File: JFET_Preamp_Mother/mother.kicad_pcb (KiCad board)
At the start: 2 copper layers, 80 x 120 mm, 90 parts, among them J101 Conn_01x02, J102 Conn_01x08_Socket, J201 XLR3, J301 XLR3, J401 XLR3, J501 XLR3, Q201 2SK209, Q202 2SK209, Q203 2SK209, Q301 2SK209, Q302 2SK209, Q303 2SK209, Q401 2SK209, Q402 2SK209, Q403 2SK209, Q501 2SK209, Q502 2SK209, Q503 2SK209, U101 PCM1865DBTR, U102 TLV70012_SOT23-5

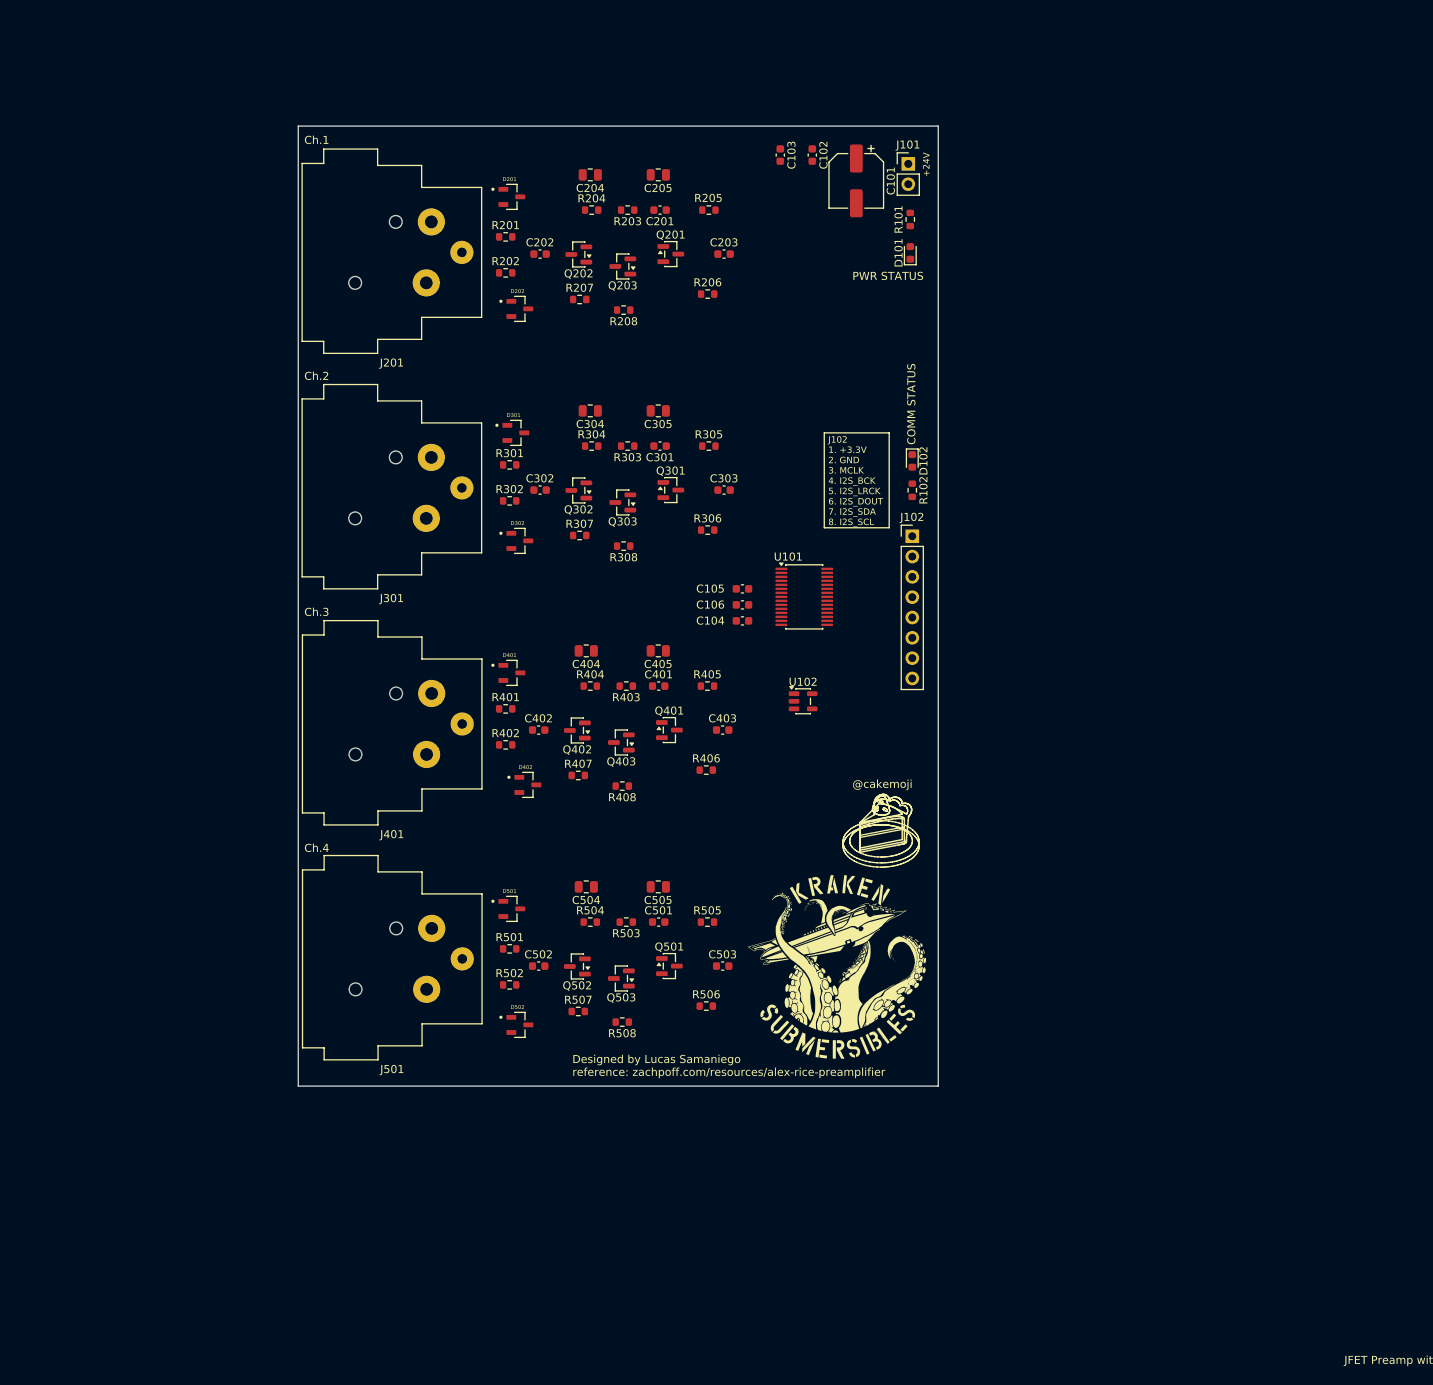
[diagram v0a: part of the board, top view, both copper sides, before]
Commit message: fix ERC on schematic, then proceed to begin routing on pcb
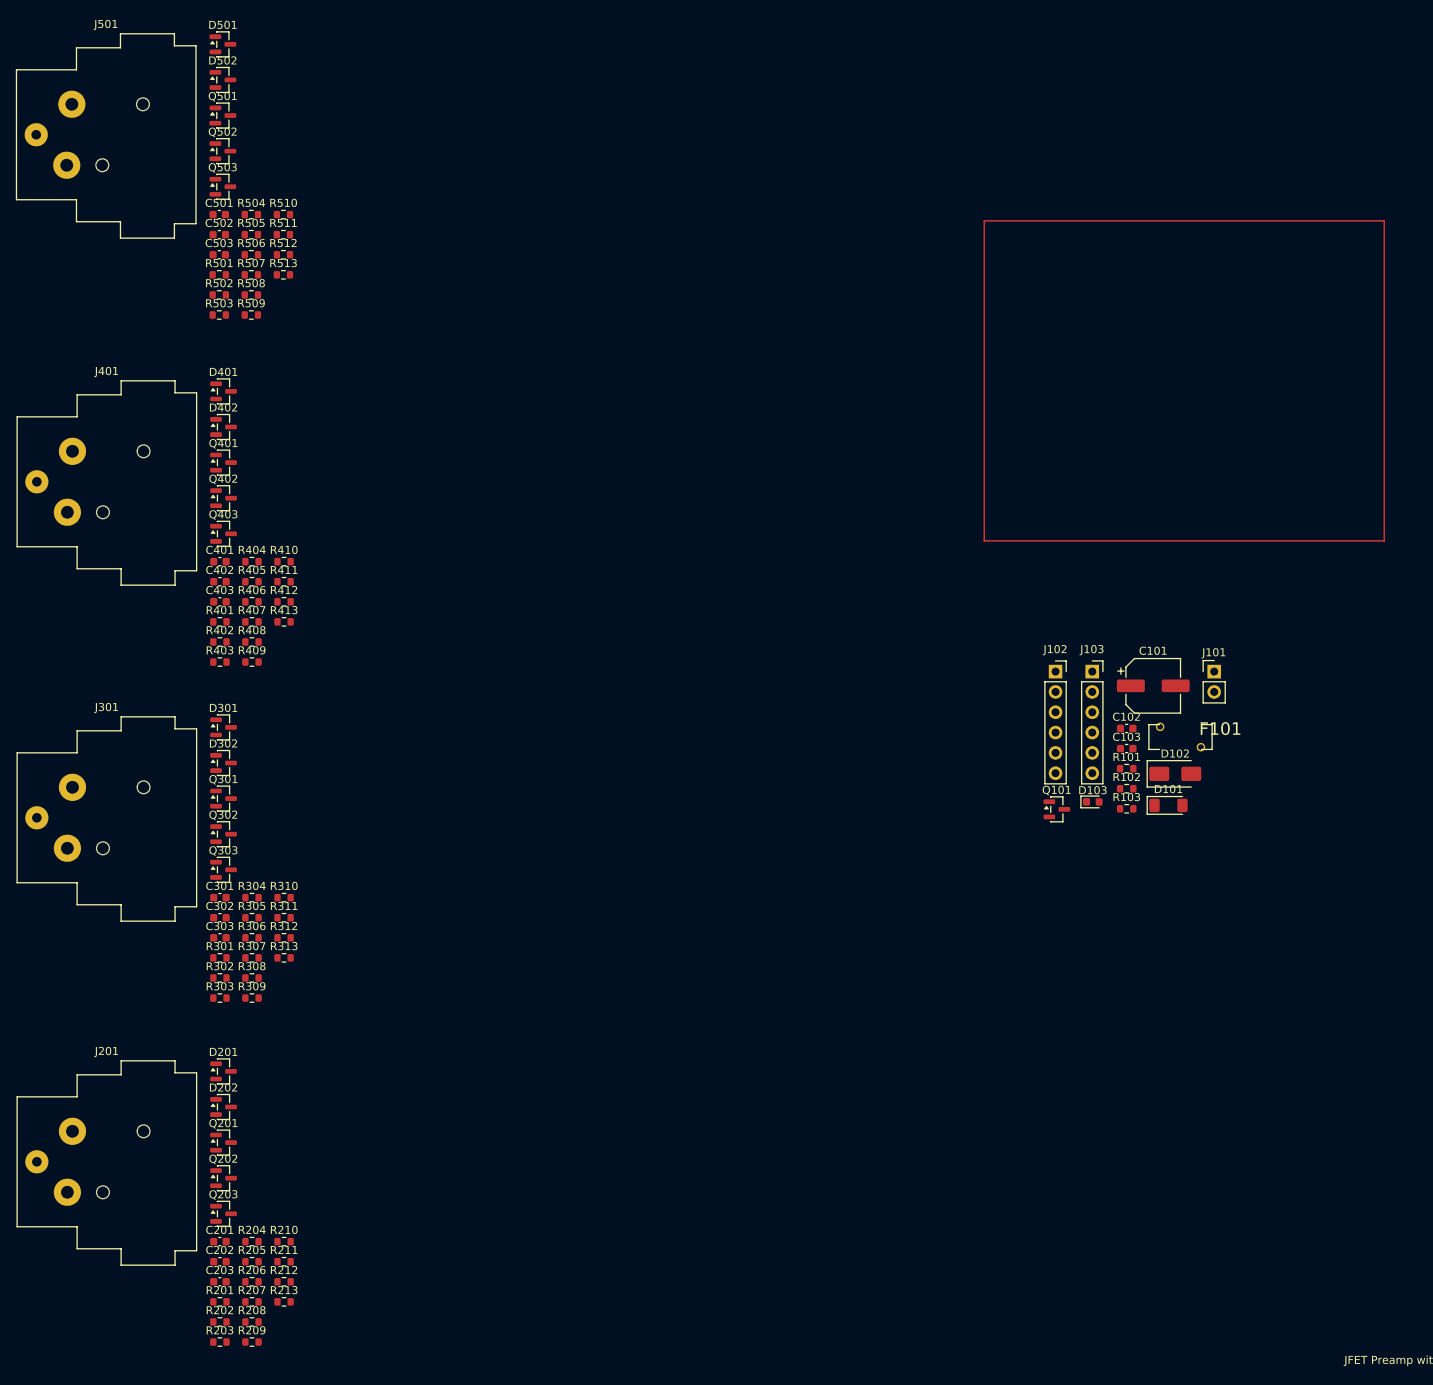
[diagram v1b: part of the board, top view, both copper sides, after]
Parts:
- removed C104: 1u, Capacitor_SMD:C_0603_1608Metric
- removed C105: 100n, Capacitor_SMD:C_0603_1608Metric
- removed C106: 2.2u, Capacitor_SMD:C_0603_1608Metric
- removed C204, C205, C304, C305, C404, C405, C504, C505: 10u, Capacitor_SMD:C_0805_2012Metric
- removed U101: PCM1865DBTR, Package_SO:TSSOP-30_4.4x7.8mm_P0.5mm
- removed U102: TLV70012_SOT23-5, Package_TO_SOT_SMD:SOT-23-5
- added D103: LED, LED_SMD:LED_0603_1608Metric, F.Cu at (158.6, 119.6)
- added F101: 0.5, downloaded_footprints:FUSRB510W51L790T310H1370, F.Cu at (169.5, 111.5)
- added J103: Conn_01x06_Socket, Connector_PinSocket_2.54mm:PinSocket_1x06_P2.54mm_Vertical, F.Cu at (158.5, 103.3)
- added Q101: AO3401A, Package_TO_SOT_SMD:SOT-23, F.Cu at (154.1, 120.6)
- added R103: 4.7k, Resistor_SMD:R_0603_1608Metric, F.Cu at (162.8, 120.5)
- added R209: 6.81k, Resistor_SMD:R_0603_1608Metric, F.Cu at (53.5, 187.1)
- added R210: 3M, Resistor_SMD:R_0603_1608Metric, F.Cu at (57.5, 174.6)
- added R211: 0, Resistor_SMD:R_0603_1608Metric, F.Cu at (57.5, 177.1)
- added R212: 0, Resistor_SMD:R_0603_1608Metric, F.Cu at (57.5, 179.6)
- added R213: 0, Resistor_SMD:R_0603_1608Metric, F.Cu at (57.5, 182.1)
- added R309: 6.81k, Resistor_SMD:R_0603_1608Metric, F.Cu at (53.5, 144.1)
- added R310: 3M, Resistor_SMD:R_0603_1608Metric, F.Cu at (57.5, 131.6)
- added R311: 0, Resistor_SMD:R_0603_1608Metric, F.Cu at (57.5, 134.1)
- added R312: 0, Resistor_SMD:R_0603_1608Metric, F.Cu at (57.5, 136.6)
- added R313: 0, Resistor_SMD:R_0603_1608Metric, F.Cu at (57.5, 139.1)
- added R409: 6.81k, Resistor_SMD:R_0603_1608Metric, F.Cu at (53.5, 102.1)
- added R410: 3M, Resistor_SMD:R_0603_1608Metric, F.Cu at (57.5, 89.6)
- added R411: 0, Resistor_SMD:R_0603_1608Metric, F.Cu at (57.5, 92.1)
- added R412: 0, Resistor_SMD:R_0603_1608Metric, F.Cu at (57.5, 94.6)
- added R413: 0, Resistor_SMD:R_0603_1608Metric, F.Cu at (57.5, 97.1)
- added R509: 6.81k, Resistor_SMD:R_0603_1608Metric, F.Cu at (53.4, 58.8)
- added R510: 3M, Resistor_SMD:R_0603_1608Metric, F.Cu at (57.4, 46.2)
- added R511: 0, Resistor_SMD:R_0603_1608Metric, F.Cu at (57.4, 48.7)
- added R512: 0, Resistor_SMD:R_0603_1608Metric, F.Cu at (57.4, 51.2)
- added R513: 0, Resistor_SMD:R_0603_1608Metric, F.Cu at (57.4, 53.7)
- D101: value LED -> BZV55C27; footprint LED_SMD:LED_0603_1608Metric -> Diode_SMD:D_MiniMELF
- D102: value LED -> SMAJ26A; footprint LED_SMD:LED_0603_1608Metric -> Diode_SMD:D_SMA
- D201, D202, D301, D302, D401, D402, D501, D502: footprint MMBZ27VALT1G:SOT95P237X111-3N -> Package_TO_SOT_SMD:SOT-23
- J102: value Conn_01x08_Socket -> Conn_01x06_Socket; footprint Connector_PinHeader_2.54mm:PinHeader_1x08_P2.54mm_Vertical -> Connector_PinSocket_2.54mm:PinSocket_1x06_P2.54mm_Vertical
- R101: value 4.7k -> 100k
- R102: value 2.2k -> 0
- R203, R303, R403, R503: value 150 -> 3M
- R205, R305, R405, R505: value 3M -> 6.81k
- R206, R306, R406, R506: value 3M -> 470
- R207, R307, R407, R507: value 3M -> 150
- R208, R308, R408, R508: value 470 -> 3M
- moved R203 150.4 mm to (49.5, 187.1), turned to 0 degrees
- moved R205 143.3 mm to (53.5, 177.1)
- moved C203 143.1 mm to (49.5, 179.6)
- moved C201 140.2 mm to (49.5, 174.6), turned to 0 degrees
- moved R201 137.8 mm to (49.5, 182.1)
- moved R206 136.0 mm to (53.5, 179.6)
- moved R202 135.9 mm to (49.5, 184.6)
- moved R204 135.8 mm to (53.5, 174.6)
- moved R208 134.7 mm to (53.5, 184.6), turned to 0 degrees
- moved C202 132.2 mm to (49.5, 177.1)
- moved R207 131.8 mm to (53.5, 182.1)
- moved Q203 128.5 mm to (49.9, 171.1), turned to 0 degrees
- moved Q201 124.3 mm to (49.9, 162.2)
- moved D502 123.8 mm to (49.8, 29.4)
- moved Q202 123.7 mm to (49.9, 166.7), turned to 0 degrees
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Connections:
- C101 pad 1: +24V -> Net-(D102-A2)
- C102 pad 1: +24V -> Net-(D102-A2)
- C103 pad 1: +24V -> Net-(D102-A2)
- C201 pad 1: Net-(C201-Pad1) -> /Channel_1/D_TVS_HOT
- C201 pad 2: Net-(Q201-D) -> Net-(Q201-G)
- C202 pad 2: Net-(Q202-G) -> /CH1_COLD
- C203 pad 1: Net-(Q201-G) -> Net-(Q203-G)
- C203 pad 2: Net-(C203-Pad2) -> Net-(D202-A2)
- C301 pad 1: Net-(C301-Pad1) -> /Channel_2/D_TVS_HOT
- C301 pad 2: Net-(Q301-D) -> Net-(Q301-G)
- C302 pad 2: Net-(Q302-G) -> /CH2_COLD
- C303 pad 1: Net-(Q301-G) -> Net-(Q303-G)
- C303 pad 2: Net-(C303-Pad2) -> Net-(D302-A2)
- C401 pad 1: Net-(C401-Pad1) -> /Channel_3/D_TVS_HOT
- C401 pad 2: Net-(Q401-D) -> Net-(Q401-G)
- C402 pad 2: Net-(Q402-G) -> /CH3_COLD
- C403 pad 1: Net-(Q401-G) -> Net-(Q403-G)
- C403 pad 2: Net-(C403-Pad2) -> Net-(D402-A2)
- C501 pad 1: Net-(C501-Pad1) -> /Channel_4/D_TVS_HOT
- C501 pad 2: Net-(Q501-D) -> Net-(Q501-G)
- C502 pad 2: Net-(Q502-G) -> /CH4_COLD
- C503 pad 1: Net-(Q501-G) -> Net-(Q503-G)
- C503 pad 2: Net-(C503-Pad2) -> Net-(D502-A2)
- D102 pad 2: Net-(D102-A) -> Net-(D102-A2)
- D201 pad 1: GND -> /CH1_GND
- D201 pad 2: +24V -> /Channel_1/D_TVS_HOT
- D202 pad 1: GND -> /CH1_GND
- D202 pad 2: +24V -> Net-(D202-A2)
- D301 pad 1: GND -> /CH2_GND
- D301 pad 2: +24V -> /Channel_2/D_TVS_HOT
- D302 pad 1: GND -> /CH2_GND
- D302 pad 2: +24V -> Net-(D302-A2)
- D401 pad 1: GND -> /CH3_GND
- D401 pad 2: +24V -> /Channel_3/D_TVS_HOT
- D402 pad 1: GND -> /CH3_GND
- D402 pad 2: +24V -> Net-(D402-A2)
- D501 pad 1: GND -> /CH4_GND
- D501 pad 2: +24V -> /Channel_4/D_TVS_HOT
- D502 pad 1: GND -> /CH4_GND
- D502 pad 2: +24V -> Net-(D502-A2)
- J101 pad 1: +24V -> Net-(J101-Pin_1)
- J102 pad 1: +3.3V -> /CH3_COLD
- J102 pad 2: GND -> /CH4_COLD
- J102 pad 3: /MCLK -> /CH3_GND
- J102 pad 4: /I2S_BCK -> /CH4_GND
- J102 pad 5: /I2S_LRCK -> /CH3_HOT
- J102 pad 6: /I2S_DOUT -> /CH4_HOT
- J201 pad 1: GND -> Net-(J201-Pad1)
- J201 pad 2: +24V -> Net-(J201-Pad2)
- J201 pad 3: +24V -> /Channel_1/D_TVS_COLD
- J301 pad 1: GND -> Net-(J301-Pad1)
- J301 pad 2: +24V -> Net-(J301-Pad2)
- J301 pad 3: +24V -> /Channel_2/D_TVS_COLD
- J401 pad 1: GND -> Net-(J401-Pad1)
- J401 pad 2: +24V -> Net-(J401-Pad2)
- J401 pad 3: +24V -> /Channel_3/D_TVS_COLD
- J501 pad 1: GND -> Net-(J501-Pad1)
- J501 pad 2: +24V -> Net-(J501-Pad2)
- J501 pad 3: +24V -> /Channel_4/D_TVS_COLD
- Q201 pad 2: Net-(Q201-D) -> /CH1_HOT
- Q202 pad 1: Net-(Q201-S) -> Net-(Q202-S)
- Q202 pad 2: /CH1_HOT -> Net-(Q201-S)
- Q202 pad 3: Net-(Q202-G) -> /CH1_GND
- Q203 pad 1: Net-(Q203-S) -> Net-(Q201-S)
- Q203 pad 2: Net-(Q201-S) -> /CH1_COLD
- Q203 pad 3: GND -> Net-(Q203-G)
- Q301 pad 2: Net-(Q301-D) -> /CH2_HOT
- Q302 pad 1: Net-(Q301-S) -> Net-(Q302-S)
- Q302 pad 2: /CH2_HOT -> Net-(Q301-S)
- Q302 pad 3: Net-(Q302-G) -> /CH2_GND
- Q303 pad 1: Net-(Q303-S) -> Net-(Q301-S)
- Q303 pad 2: Net-(Q301-S) -> /CH2_COLD
- Q303 pad 3: GND -> Net-(Q303-G)
- Q401 pad 2: Net-(Q401-D) -> /CH3_HOT
- Q402 pad 1: Net-(Q401-S) -> Net-(Q402-S)
- Q402 pad 2: /CH3_HOT -> Net-(Q401-S)
- Q402 pad 3: Net-(Q402-G) -> /CH3_GND
- Q403 pad 1: Net-(Q403-S) -> Net-(Q401-S)
- Q403 pad 2: Net-(Q401-S) -> /CH3_COLD
- Q403 pad 3: GND -> Net-(Q403-G)
- Q501 pad 2: Net-(Q501-D) -> /CH4_HOT
- Q502 pad 1: Net-(Q501-S) -> Net-(Q502-S)
- Q502 pad 2: /CH4_HOT -> Net-(Q501-S)
- Q502 pad 3: Net-(Q502-G) -> /CH4_GND
- Q503 pad 1: Net-(Q503-S) -> Net-(Q501-S)
- Q503 pad 2: Net-(Q501-S) -> /CH4_COLD
- Q503 pad 3: GND -> Net-(Q503-G)
- R101 pad 1: Net-(D101-A) -> Net-(D102-A2)
- R101 pad 2: +24V -> Net-(D101-A)
- R102 pad 1: Net-(D102-A) -> +24V
- R102 pad 2: /I2S_DOUT -> Net-(D102-A2)
- R201 pad 2: Net-(C202-Pad1) -> /Channel_1/D_TVS_HOT
- R202 pad 2: Net-(C203-Pad2) -> Net-(D202-A2)
- R203 pad 2: Net-(C201-Pad1) -> Net-(Q201-G)
- R204 pad 1: Net-(C204-Pad2) -> Net-(Q201-G)
- R204 pad 2: Net-(Q202-G) -> /CH1_GND
- R205 pad 1: Net-(Q201-D) -> /CH1_HOT
- R205 pad 2: Net-(Q201-G) -> +24V
- R206 pad 1: Net-(Q201-G) -> Net-(Q202-S)
- R206 pad 2: GND -> /CH1_GND
- R207 pad 1: Net-(Q202-G) -> /CH1_HOT
- R207 pad 2: GND -> Net-(C202-Pad1)
- R208 pad 1: Net-(Q203-S) -> Net-(Q203-G)
- R208 pad 2: GND -> /CH1_GND
- R301 pad 2: Net-(C302-Pad1) -> /Channel_2/D_TVS_HOT
- R302 pad 2: Net-(C303-Pad2) -> Net-(D302-A2)
- R303 pad 2: Net-(C301-Pad1) -> Net-(Q301-G)
- R304 pad 1: Net-(C304-Pad2) -> Net-(Q301-G)
- R304 pad 2: Net-(Q302-G) -> /CH2_GND
- R305 pad 1: Net-(Q301-D) -> /CH2_HOT
- R305 pad 2: Net-(Q301-G) -> +24V
- R306 pad 1: Net-(Q301-G) -> Net-(Q302-S)
- R306 pad 2: GND -> /CH2_GND
- R307 pad 1: Net-(Q302-G) -> /CH2_HOT
- R307 pad 2: GND -> Net-(C302-Pad1)
- R308 pad 1: Net-(Q303-S) -> Net-(Q303-G)
- R308 pad 2: GND -> /CH2_GND
- R401 pad 2: Net-(C402-Pad1) -> /Channel_3/D_TVS_HOT
- R402 pad 2: Net-(C403-Pad2) -> Net-(D402-A2)
- R403 pad 2: Net-(C401-Pad1) -> Net-(Q401-G)
- R404 pad 1: Net-(C404-Pad2) -> Net-(Q401-G)
- R404 pad 2: Net-(Q402-G) -> /CH3_GND
- R405 pad 1: Net-(Q401-D) -> /CH3_HOT
- R405 pad 2: Net-(Q401-G) -> +24V
- R406 pad 1: Net-(Q401-G) -> Net-(Q402-S)
- R406 pad 2: GND -> /CH3_GND
- R407 pad 1: Net-(Q402-G) -> /CH3_HOT
- R407 pad 2: GND -> Net-(C402-Pad1)
- R408 pad 1: Net-(Q403-S) -> Net-(Q403-G)
- R408 pad 2: GND -> /CH3_GND
- R501 pad 2: Net-(C502-Pad1) -> /Channel_4/D_TVS_HOT
- R502 pad 2: Net-(C503-Pad2) -> Net-(D502-A2)
- R503 pad 2: Net-(C501-Pad1) -> Net-(Q501-G)
- R504 pad 1: Net-(C504-Pad2) -> Net-(Q501-G)
- R504 pad 2: Net-(Q502-G) -> /CH4_GND
- R505 pad 1: Net-(Q501-D) -> /CH4_HOT
- R505 pad 2: Net-(Q501-G) -> +24V
- R506 pad 1: Net-(Q501-G) -> Net-(Q502-S)
- R506 pad 2: GND -> /CH4_GND
- R507 pad 1: Net-(Q502-G) -> /CH4_HOT
- R507 pad 2: GND -> Net-(C502-Pad1)
- R508 pad 1: Net-(Q503-S) -> Net-(Q503-G)
- R508 pad 2: GND -> /CH4_GND
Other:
- board outline removed
- board text removed: "+24V"
- board text removed: "@cakemoji"
- board text removed: "COMM STATUS"
- board text removed: "Ch.1"
- board text removed: "Ch.2"
- board text removed: "Ch.3"
- board text removed: "Ch.4"
- board text removed: "Designed by Lucas Samaniego reference: zachpoff.com/resources/alex-rice-preamplifier"
- board text removed: "J102 1. +3.3V 2. GND 3. MCLK 4. I2S_BCK 5. I2S_LRCK 6. I2S_DOUT 7. I2S_SDA 8. I2S_SCL"
- board text removed: "PWR STATUS"

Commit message: WIP motherboard pcb save point, layout and partial routing complete
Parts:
- D102: value SMAJ26A -> SMAJ26CA
- moved R103 110.6 mm to (103.7, 27.0)
- moved R102 109.2 mm to (108.5, 23.2), turned to -90 degrees
- moved D103 101.7 mm to (104.0, 33.8), turned to 90 degrees
- moved C103 101.0 mm to (108.5, 27.8), turned to -90 degrees
- moved D101 98.7 mm to (134.5, 27.2), turned to -90 degrees
- moved D102 97.4 mm to (128.5, 27.5), turned to 90 degrees
- moved Q101 96.7 mm to (139.6, 24.9), turned to 180 degrees
- moved C102 96.5 mm to (113.0, 27.8), turned to -90 degrees
- moved C101 90.0 mm to (120.0, 27.8), turned to -90 degrees
- moved F101 88.1 mm to (146.5, 26.5)
- moved R101 87.5 mm to (140.5, 30.8), turned to -90 degrees
- moved J101 79.9 mm to (154.0, 26.0)
- moved R209 74.6 mm to (77.0, 116.3), turned to -90 degrees
- moved R202 72.8 mm to (54.2, 112.0), turned to 180 degrees
- moved R203 71.3 mm to (62.2, 117.0), turned to 180 degrees
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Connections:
- C101 pad 1: Net-(D102-A2) -> /Q101_Drain
- C102 pad 1: Net-(D102-A2) -> /Q101_Drain
- C103 pad 1: Net-(D102-A2) -> /Q101_Drain
- D101 pad 1: GND -> /Q101_Drain
- D102 pad 2: Net-(D102-A2) -> /Q101_Drain
- Q101 pad 3: Net-(D102-A2) -> /Q101_Drain
- R101 pad 1: Net-(D102-A2) -> Net-(D101-A)
- R101 pad 2: Net-(D101-A) -> GND
- R102 pad 2: Net-(D102-A2) -> /Q101_Drain
- R103 pad 2: Net-(D102-A2) -> /Q101_Drain
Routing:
- net Net-(D502-A2): track 0.00 -> 60.0 mm
- net /Channel_2/D_TVS_HOT: track 0.00 -> 17.7 mm
- net /Channel_4/D_TVS_HOT: track 0.00 -> 17.7 mm
- net /Channel_3/D_TVS_HOT: track 0.00 -> 17.7 mm
- net /Channel_1/D_TVS_HOT: track 0.00 -> 17.7 mm
- net Net-(Q201-G): track 0.00 -> 16.0 mm
- net Net-(Q501-G): track 0.00 -> 16.0 mm
- net Net-(Q401-G): track 0.00 -> 16.0 mm
- net Net-(Q301-G): track 0.00 -> 16.0 mm
- net Net-(Q303-G): track 0.00 -> 16.0 mm
- net Net-(Q203-G): track 0.00 -> 16.0 mm
- net Net-(Q503-G): track 0.00 -> 16.0 mm
- net Net-(Q403-G): track 0.00 -> 16.0 mm
- net Net-(Q301-S): track 0.00 -> 15.5 mm
- net Net-(Q501-S): track 0.00 -> 15.5 mm
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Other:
- board outline added: 140 x 120 mm

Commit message: finished pcb, updated schematic formatting, ready for fab
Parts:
- moved J103 42.8 mm to (114.7, 96.0)
- moved J102 40.9 mm to (127.3, 60.0)
- moved F101 0.08 mm to (146.5, 26.6)
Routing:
- net +24V: track 0.00 -> 262.7 mm, vias 0 -> 12
- net /CH1_GND: track 9.88 -> 123.2 mm, vias 6 -> 2
- net /CH3_GND: track 9.88 -> 117.2 mm, vias 6 -> 8
- net /CH4_GND: track 11.4 -> 110.8 mm, vias 7 -> 4
- net /CH2_GND: track 9.88 -> 107.4 mm, vias 6 -> 2
- net /CH1_HOT: track 12.2 -> 78.2 mm, vias 0 -> 4
- net /CH2_HOT: track 12.2 -> 76.5 mm, vias 0 -> 4
- net /CH3_COLD: track 9.26 -> 69.3 mm, vias 0 -> 4
- net /CH4_HOT: track 12.2 -> 67.4 mm, vias 0 -> 2
- net /CH4_COLD: track 15.1 -> 69.7 mm, vias 0 -> 2
- net /CH1_COLD: track 9.26 -> 62.1 mm, vias 0 -> 4
- net /CH3_HOT: track 12.2 -> 62.4 mm, vias 0 -> 4
- net /CH2_COLD: track 9.26 -> 56.8 mm, vias 0 -> 2
- net Net-(D302-A2): track 11.4 -> 58.7 mm, vias 0 -> 2
- net Net-(D402-A2): track 11.4 -> 58.5 mm, vias 0 -> 2
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- added copper zone on B.Cu, net GND
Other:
- board text added: "+24V"
- board text added: "5/3/2026"
- board text added: "Designed by: Lucas Samaniego ref: zachpoff.com/resources/alex-rice-piezo-preamplifier/"
- board text added: "JFET PREAMP & ADC DAUGHTERBOARD"
- board text added: "JFET Preamp & ADC Motherboard"
- board text added: "JFET Preamp with ADC Motherboard By Lucas Samaniego"
- board text added: "PWR STATUS"
- board text removed: "JFET Preamp with ADC PCB By Lucas Samaniego"
